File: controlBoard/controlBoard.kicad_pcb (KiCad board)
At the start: 2 copper layers, 15 parts, among them J1 FTDI, J2 Servo, J3 Fingerprint, J4 Barrel_Jack_Switch_MountingPin, J5 ICSP, U4 ATmega328P-AU, U5 PCA9685BS, Y1 Crystal

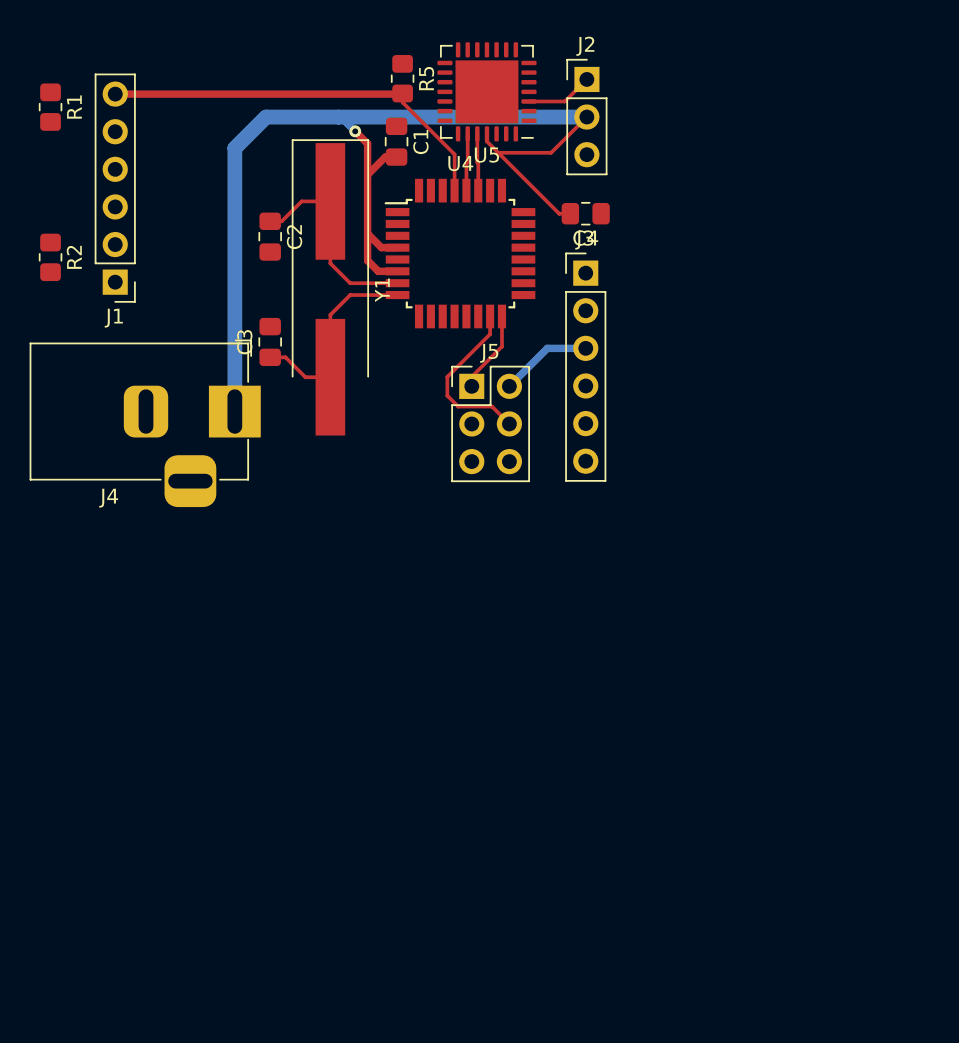
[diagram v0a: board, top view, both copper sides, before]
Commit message: Added button footprint and layout pcb
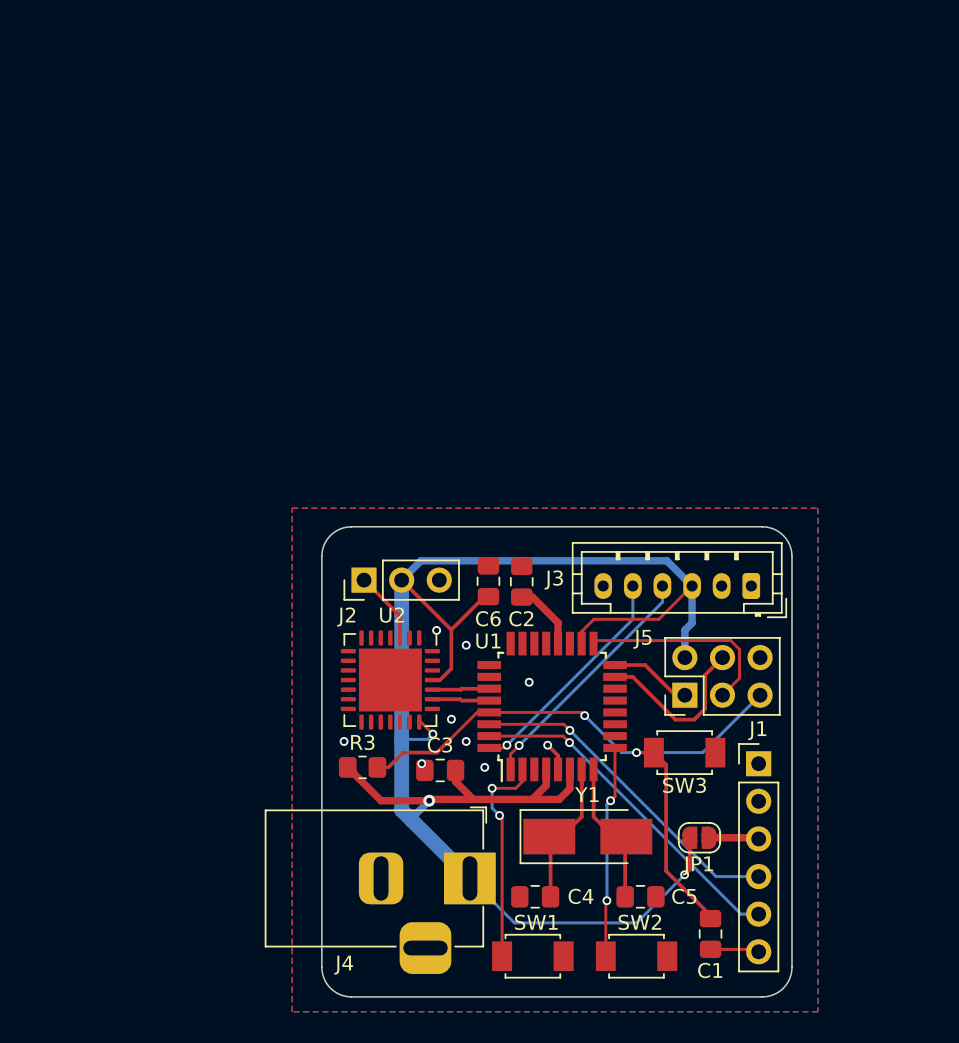
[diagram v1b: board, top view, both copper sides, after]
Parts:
- removed R1, R2: 10k, Resistor_SMD:R_0805_2012Metric_Pad1.20x1.40mm_HandSolder
- added C1: 100n, Capacitor_SMD:C_0805_2012Metric_Pad1.18x1.45mm_HandSolder, F.Cu at (167.0, 96.8)
- added C2: 100n, Capacitor_SMD:C_0805_2012Metric_Pad1.18x1.45mm_HandSolder, F.Cu at (154.2, 73.0)
- added JP1: JVCC, Jumper:SolderJumper-2_P1.3mm_Open_RoundedPad1.0x1.5mm, F.Cu at (166.2, 90.2)
- added SW1: SW_Push, bidpl:SMD_Pushbutton_3mmx4mm, F.Cu at (155.0, 98.2)
- added SW2: SW_Push, bidpl:SMD_Pushbutton_3mmx4mm, F.Cu at (162.0, 98.2)
- added SW3: SW_Push, bidpl:SMD_Pushbutton_3mmx4mm, F.Cu at (165.2, 84.5)
- J3: footprint Connector_PinHeader_2.54mm:PinHeader_1x06_P2.54mm_Vertical -> Connector_JST:JST_PH_B6B-PH-K_1x06_P2.00mm_Vertical
- Y1: footprint Crystal:Crystal_SMD_HC49-SD_HandSoldering -> Crystal:Crystal_SMD_5032-2Pin_5.0x3.2mm_HandSoldering
- moved J1 54.3 mm to (170.2, 85.2), turned to 0 degrees
- moved C4 48.0 mm to (155.2, 94.2), turned to 180 degrees
- moved R3 46.6 mm to (143.5, 85.5), turned to 0 degrees
- moved C5 45.0 mm to (162.3, 94.2), turned to 0 degrees
- moved C3 42.6 mm to (148.7, 85.7), turned to 0 degrees
- moved Y1 40.8 mm to (158.7, 90.2), turned to 0 degrees
- moved U2 40.3 mm to (145.4, 79.6), turned to 270 degrees
- moved J2 37.0 mm to (143.6, 72.9), turned to 90 degrees
- moved J4 35.3 mm to (150.8, 93.0)
- moved U1 31.2 mm to (156.3, 81.4), turned to 90 degrees
- moved C6 25.7 mm to (152.0, 72.9), turned to 270 degrees
- moved J5 25.3 mm to (165.3, 80.6), turned to 90 degrees
- moved J3 23.9 mm to (169.8, 73.2), turned to 180 degrees
- renumbered C1 to C3, C2 to C4, C3 to C5, C4 to C6, R5 to R3, U4 to U1, U5 to U2
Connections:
- J1 pad 3: +5V -> Net-(J1-Pad3)
- J1 pad 6: /RESET -> Net-(C1-Pad2)
- U1 pad 20: (no net) -> Net-(C2-Pad1)
- U2 pad 1: (no net) -> GND
- U2 pad 2: (no net) -> GND
- U2 pad 21: (no net) -> +5V
- U2 pad 22: (no net) -> GND
- U2 pad 26: (no net) -> GND
- U2 pad 27: (no net) -> GND
- U2 pad 28: (no net) -> GND
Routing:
- net +5V: track 81.6 -> 117.4 mm, vias 1 -> 3
- net /TX: track 0.00 -> 23.2 mm, vias 0 -> 1
- net /RX: track 0.00 -> 22.5 mm, vias 0 -> 1
- net /RESET: track 27.4 -> 44.1 mm, vias 0 -> 2
- net /TX1: track 0.00 -> 16.6 mm, vias 0 -> 1
- net /RX1: track 0.00 -> 15.5 mm, vias 0 -> 1
- net /Q: track 0.00 -> 14.7 mm, vias 0 -> 2
- net /Q': track 0.00 -> 14.3 mm, vias 0 -> 2
- net /SCK: track 0.00 -> 13.8 mm
- net /XTAL-: track 14.5 -> 9.19 mm
- net /XTAL+: track 15.0 -> 10.2 mm
- net Net-(C2-Pad1): track 0.00 -> 4.58 mm
- net Net-(J1-Pad3): track 0.00 -> 3.38 mm
- net Net-(C1-Pad2): track 0.00 -> 3.32 mm
- net GND: track 0.00 -> 1.93 mm, vias 0 -> 9
- added copper zone on B.Cu, net GND
- added copper zone on F.Cu, net GND
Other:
- board outline added: 31.8 x 31.8 mm

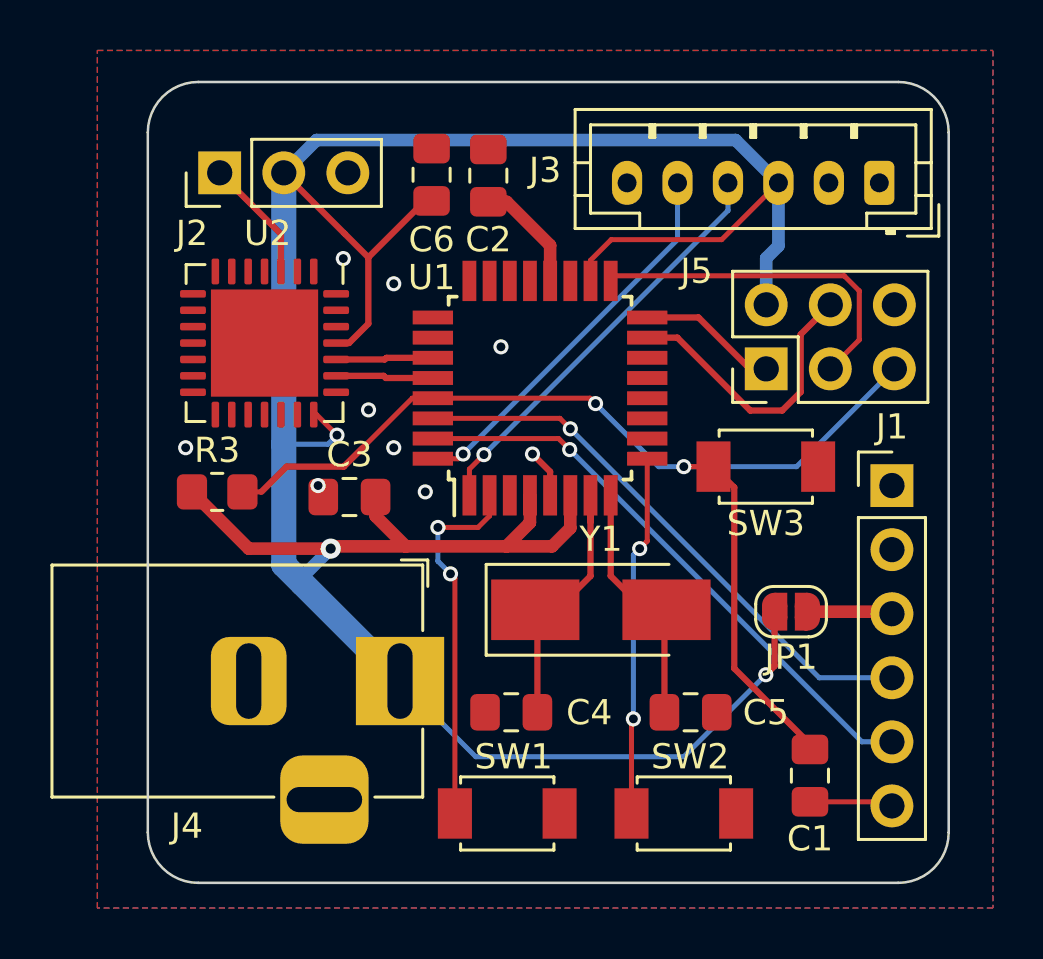
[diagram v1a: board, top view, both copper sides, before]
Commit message: Swapped TX1 and RX1 pins, cleaned up board a bit to send off to production
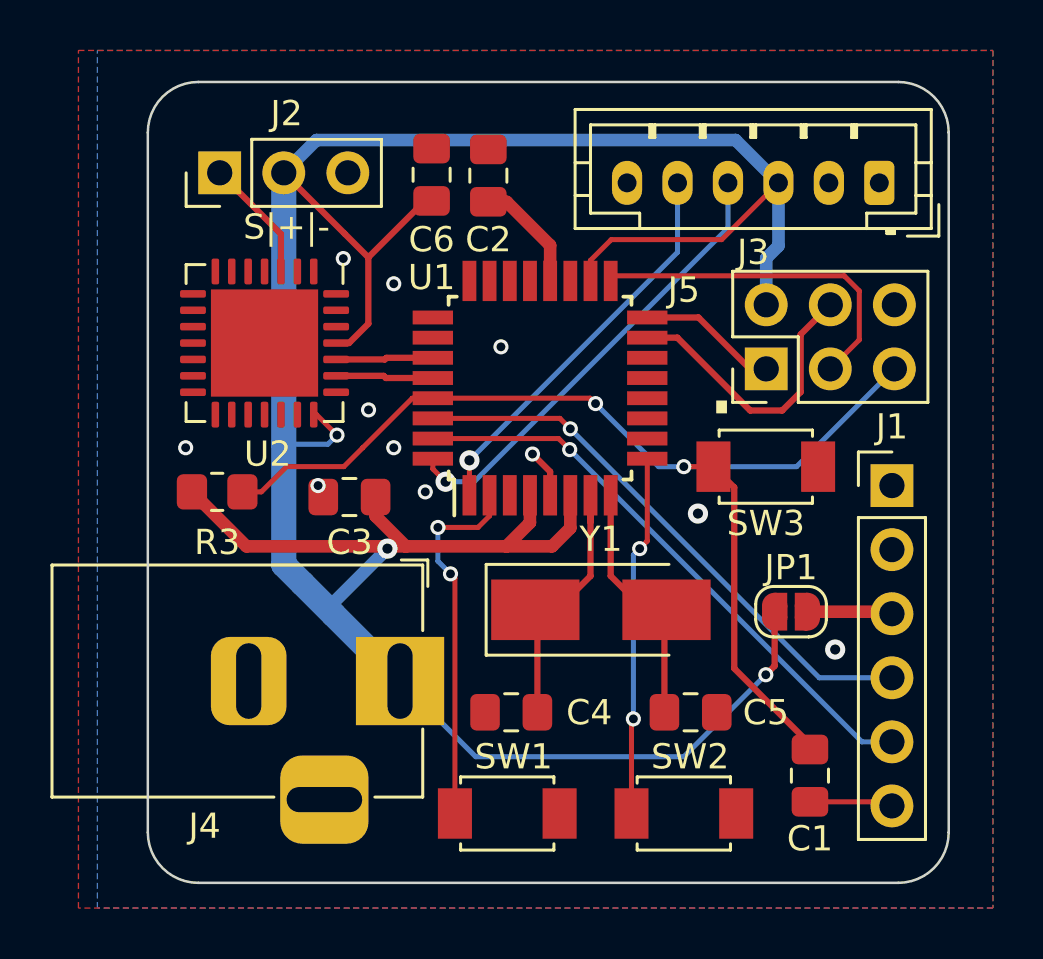
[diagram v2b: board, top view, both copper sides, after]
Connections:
- J1 pad 2: (no net) -> Net-(J1-Pad2)
- J3 pad 1: (no net) -> Net-(J3-Pad1)
- J3 pad 2: (no net) -> Net-(J3-Pad2)
- J4 pad 3: (no net) -> Net-(J4-Pad3)
- U1 pad 1: /TX1 -> /RX1
- U1 pad 10: (no net) -> Net-(U1-Pad10)
- U1 pad 11: (no net) -> Net-(U1-Pad11)
- U1 pad 12: (no net) -> Net-(U1-Pad12)
- U1 pad 13: (no net) -> Net-(U1-Pad13)
- U1 pad 14: (no net) -> Net-(U1-Pad14)
- U1 pad 19: (no net) -> Net-(U1-Pad19)
- U1 pad 22: (no net) -> Net-(U1-Pad22)
- U1 pad 23: (no net) -> Net-(U1-Pad23)
- U1 pad 24: (no net) -> Net-(U1-Pad24)
- U1 pad 25: (no net) -> Net-(U1-Pad25)
- U1 pad 26: (no net) -> Net-(U1-Pad26)
- U1 pad 32: /RX1 -> /TX1
- U2 pad 10: (no net) -> Net-(U2-Pad10)
- U2 pad 12: (no net) -> Net-(U2-Pad12)
- U2 pad 13: (no net) -> Net-(U2-Pad13)
- U2 pad 14: (no net) -> Net-(U2-Pad14)
- U2 pad 15: (no net) -> Net-(U2-Pad15)
- U2 pad 16: (no net) -> Net-(U2-Pad16)
- U2 pad 17: (no net) -> Net-(U2-Pad17)
- U2 pad 18: (no net) -> Net-(U2-Pad18)
- U2 pad 19: (no net) -> Net-(U2-Pad19)
- U2 pad 4: (no net) -> Net-(U2-Pad4)
- U2 pad 5: (no net) -> Net-(U2-Pad5)
- U2 pad 6: (no net) -> Net-(U2-Pad6)
- U2 pad 7: (no net) -> Net-(U2-Pad7)
- U2 pad 8: (no net) -> Net-(U2-Pad8)
- U2 pad 9: (no net) -> Net-(U2-Pad9)
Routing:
- net +5V: track 117.4 -> 119.2 mm
- net /TX1: track 16.6 -> 18.3 mm
- net GND: vias 9 -> 11
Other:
- net class Default: trace_width 0.25 -> 0.2
- rule pad_to_mask_clearance: 0 -> 0.05
- board text added: "+"
- board text added: "+5V"
- board text added: "-"
- board text added: "- |MOSI| + RST|SCK|MISO"
- board text added: "."
- board text added: "Fingerprint Doorlock v1.0 UIUC 2021"
- board text added: "GND"
- board text added: "JLCJLCJLCJLC"
- board text added: "NC"
- board text added: "RST"
- board text added: "RX"
- board text added: "RX1"
- board text added: "S"
- board text added: "S|+|-"
- board text added: "TX"
- board text added: "TX1"
- board text added: "VCC"

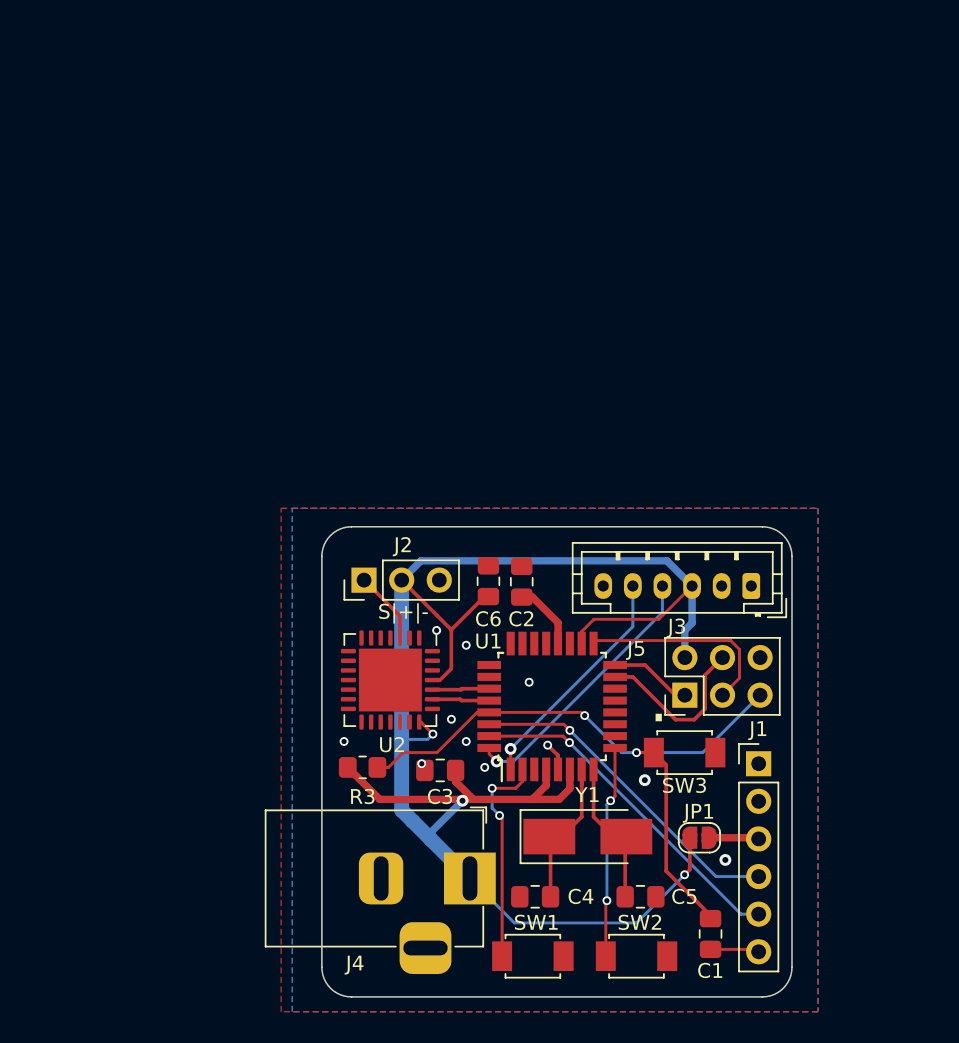
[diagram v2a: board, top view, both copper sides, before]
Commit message: Added 2 electrolytic caps, pin 13 led, 3v3 linear reg, seperated power for logic and servo, increased board size, rotated some headers, added some test points
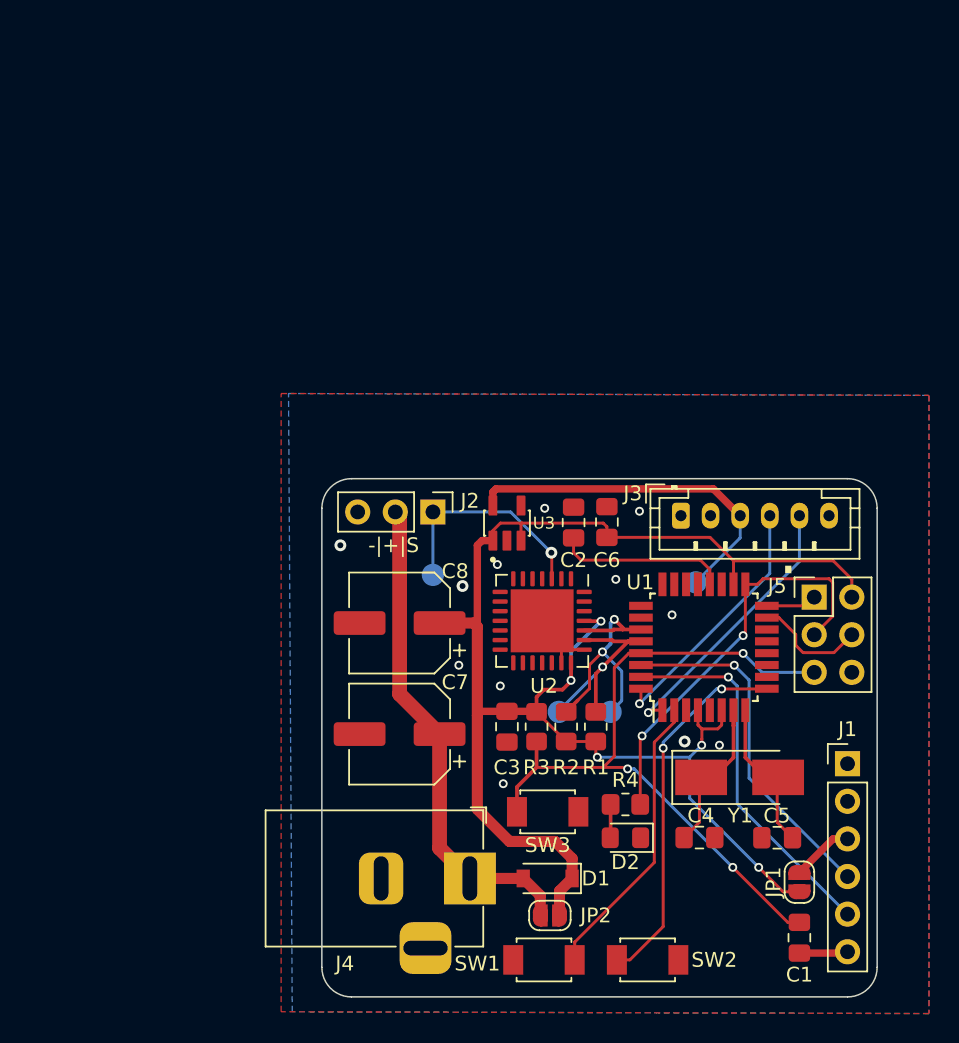
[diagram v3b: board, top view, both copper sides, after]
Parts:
- added 3V3: 3V3, TestPoint:TestPoint_Pad_D1.5mm, B.Cu at (166.0, 73.0)
- added C7: 47u, Capacitor_SMD:CP_Elec_6.3x7.7, F.Cu at (146.0, 83.2)
- added C8: 47u, Capacitor_SMD:CP_Elec_6.3x7.7, F.Cu at (146.0, 75.8)
- added D1: D_Schottky, Diode_SMD:D_SOD-123, F.Cu at (156.0, 93.0)
- added D2: LED, LED_SMD:LED_0805_2012Metric_Pad1.15x1.40mm_HandSolder, F.Cu at (161.2, 90.2)
- added JP2: JVCC, Jumper:SolderJumper-2_P1.3mm_Open_RoundedPad1.0x1.5mm, F.Cu at (156.2, 95.5)
- added PWM: PWM, TestPoint:TestPoint_Pad_D1.5mm, B.Cu at (148.2, 72.5)
- added R1: 4k7, Resistor_SMD:R_0805_2012Metric_Pad1.20x1.40mm_HandSolder, F.Cu at (159.2, 82.8)
- added R2: 4k7, Resistor_SMD:R_0805_2012Metric_Pad1.20x1.40mm_HandSolder, F.Cu at (157.2, 82.8)
- added R4: 1k, Resistor_SMD:R_0805_2012Metric_Pad1.20x1.40mm_HandSolder, F.Cu at (161.2, 88.0)
- added SCL: SCL, TestPoint:TestPoint_Pad_D1.5mm, B.Cu at (156.8, 81.8)
- added SDA: SDA, TestPoint:TestPoint_Pad_D1.5mm, B.Cu at (160.2, 81.8)
- added U3: AP2112K-3.3TRG1, AP2112K-3:SOT95P285X140-5N, F.Cu at (153.2, 69.0)
- J4: value Barrel_Jack_Switch_MountingPin -> Barrel_Jack_Switch
- moved R3 12.1 mm to (155.2, 82.8), turned to 270 degrees
- moved C4 11.8 mm to (166.2, 90.2), turned to 0 degrees
- moved U1 11.0 mm to (166.6, 77.4)
- moved U2 11.0 mm to (155.6, 75.6)
- moved Y1 11.0 mm to (169.0, 86.2)
- moved J5 11.0 mm to (174.0, 74.0), turned to 0 degrees
- moved SW3 10.1 mm to (156.0, 88.5)
- moved C5 10.1 mm to (171.5, 90.2), turned to 180 degrees
- moved C6 8.94 mm to (160.0, 68.9)
- moved JP1 7.39 mm to (173.0, 93.2), turned to 270 degrees
- moved J3 6.72 mm to (165.0, 68.5), turned to 0 degrees
- moved J2 6.54 mm to (148.2, 68.2), turned to 270 degrees
- moved C1 6.01 mm to (173.0, 97.0)
- moved J1 6.00 mm to (176.2, 85.2)
- moved C3 5.39 mm to (153.2, 82.8), turned to 90 degrees
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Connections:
- J2 pad 2: +5V -> +5VA
- J3 pad 3: +5V -> +3V3
- J4 pad 1: +5V -> +5VA
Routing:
- net +5VA: track 0.00 -> 33.4 mm
- net +3V3: track 0.00 -> 24.2 mm
- net /SCK: track 13.8 -> 28.0 mm, vias 0 -> 2
- net /SDA: track 3.86 -> 17.3 mm, vias 0 -> 2
- net /Q': track 14.3 -> 25.2 mm
- net /SCL: track 3.87 -> 14.7 mm, vias 0 -> 1
- net /PWM0: track 4.92 -> 15.2 mm, vias 0 -> 1
- net +5V: track 119.2 -> 110.9 mm, vias 3 -> 5
- net Net-(C2-Pad1): track 4.58 -> 11.7 mm
- net GND: track 1.93 -> 7.02 mm, vias 11 -> 12
- net /Q: track 14.7 -> 19.6 mm, vias 2 -> 0
- net /RESET: track 44.1 -> 48.9 mm, vias 2 -> 3
- net /MOSI: track 11.5 -> 7.65 mm
- net /RX1: track 15.8 -> 18.5 mm
- net Net-(D2-Pad2): track 0.00 -> 2.26 mm
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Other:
- board size 31.8 x 31.8 mm -> 37.5 x 35 mm
- board text added: "+ |MISO MOSI|SCK - | RST"
- board text added: "-|+|S"
- board text added: "3V3"
- board text removed: "- |MOSI| + RST|SCK|MISO"
- board text removed: "S|+|-"
